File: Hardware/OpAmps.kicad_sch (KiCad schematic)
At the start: 55 parts, among them U10 TL074, U11 TL074, U12 TL074, U13 TL074, U14 TL074

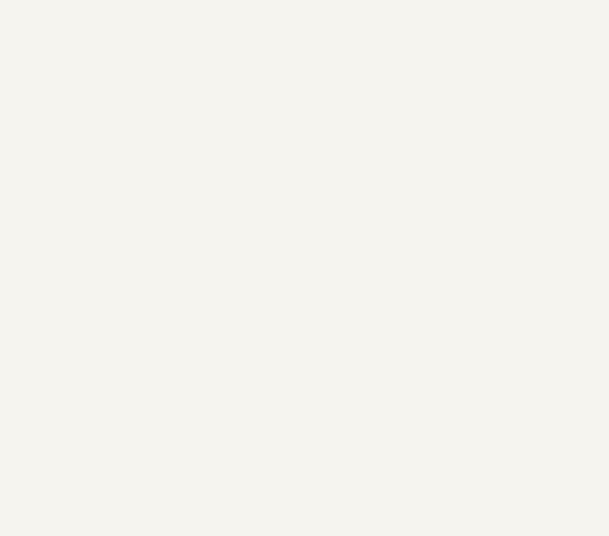
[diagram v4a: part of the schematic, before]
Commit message: Added individual audio channel breakout
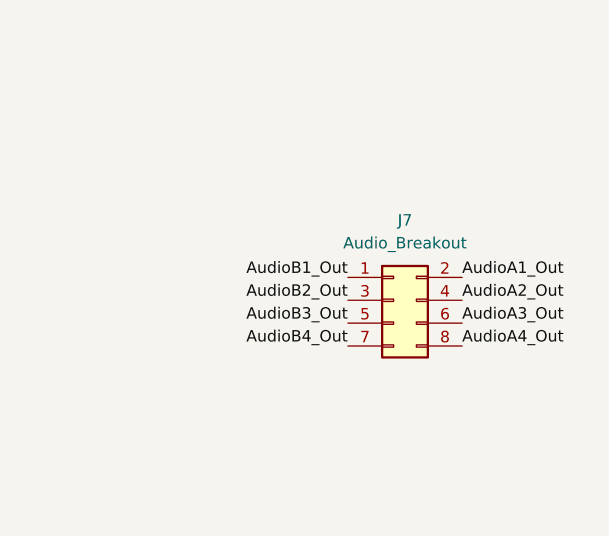
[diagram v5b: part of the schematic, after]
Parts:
- added J7: Audio_Breakout, Connector_PinHeader_2.54mm:PinHeader_2x04_P2.54mm_Vertical, symbol Connector_Generic:Conn_02x04_Odd_Even
- U14: footprint Package_SO:TSSOP-14_4.4x5mm_P0.65mm -> Package_SO:SOIC-14_3.9x8.7mm_P1.27mm
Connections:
- net AudioA1_Out: now also J7.2 (Pin_2)
- net AudioA2_Out: now also J7.4 (Pin_4)
- net AudioA3_Out: now also J7.6 (Pin_6)
- net AudioA4_Out: now also J7.8 (Pin_8)
- net AudioB1_Out: now also J7.1 (Pin_1)
- net AudioB2_Out: now also J7.3 (Pin_3)
- net AudioB3_Out: now also J7.5 (Pin_5)
- net AudioB4_Out: now also J7.7 (Pin_7)
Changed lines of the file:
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@@
     (effects (font (size 1.27 1.27)) (justify left bottom))
+  )
+  (label "AudioB1_Out" (at 358.14 184.15 180)
+    (effects (font (size 1.27 1.27)) (justify right bottom))
+  )
+  (label "AudioA3_Out" (at 370.84 189.23 0)
+    (effects (font (size 1.27 1.27)) (justify left bottom))
+  )
+  (label "AudioB3_Out" (at 358.14 189.23 180)
+    (effects (font (size 1.27 1.27)) (justify right bottom))
   )
   (label "AudioB1_Out" (at 240.03 35.56 0)
     (effects (font (size 1.27 1.27)) (justify left bottom))
   )
+  (label "AudioA2_Out" (at 370.84 186.69 0)
+    (effects (font (size 1.27 1.27)) (justify left bottom))
+  )
   (label "AudioA2_Out" (at 284.48 58.42 180)
     (effects (font (size 1.27 1.27)) (justify right bottom))
@@
     (effects (font (size 1.27 1.27)) (justify right bottom))
   )
+  (label "AudioB2_Out" (at 358.14 186.69 180)
+    (effects (font (size 1.27 1.27)) (justify right bottom))
+  )
+  (label "AudioA4_Out" (at 370.84 191.77 0)
+    (effects (font (size 1.27 1.27)) (justify left bottom))
+  )
   (label "AudioB2_Out" (at 241.3 67.31 0)
     (effects (font (size 1.27 1.27)) (justify left bottom))
@@
     (effects (font (size 1.27 1.27)) (justify left bottom))
   )
+  (label "AudioA1_Out" (at 370.84 184.15 0)
+    (effects (font (size 1.27 1.27)) (justify left bottom))
+  )
   (label "AudioA4_Out" (at 284.48 123.19 180)
     (effects (font (size 1.27 1.27)) (justify right bottom))
@@
   (label "AudioA2_Out" (at 182.88 67.31 0)
     (effects (font (size 1.27 1.27)) (justify left bottom))
+  )
+  (label "AudioB4_Out" (at 358.14 191.77 180)
+    (effects (font (size 1.27 1.27)) (justify right bottom))
   )
   (label "AudioB3_Out" (at 284.48 97.79 180)
@@
     (property "Reference" "U14" (id 0) (at 311.15 63.5 0))
     (property "Value" "TL074" (id 1) (at 311.15 71.12 0))
-    (property "Footprint" "Package_SO:TSSOP-14_4.4x5mm_P0.65mm" (id 2) (at 307.34 69.85 0)
+    (property "Footprint" "Package_SO:SOIC-14_3.9x8.7mm_P1.27mm" (id 2) (at 307.34 69.85 0)
       (effects (font (size 1.27 1.27)) hide)
     )
@@
     (pin "1")
   )
+  (symbol (lib_id "Connector_Generic:Conn_02x04_Odd_Even") (at 363.22 186.69 0) (unit 1)
+    (in_bom yes) (on_board yes) (fields_autoplaced)
+    (property "Reference" "J7" (id 0) (at 364.49 177.8 0))
+    (property "Value" "Audio_Breakout" (id 1) (at 364.49 180.34 0))
+    (property "Footprint" "Connector_PinHeader_2.54mm:PinHeader_2x04_P2.54mm_Vertical" (id 2) (at 363.22 186.69 0)
+      (effects (font (size 1.27 1.27)) hide)
+    )
+    (property "Datasheet" "~" (id 3) (at 363.22 186.69 0)
+      (effects (font (size 1.27 1.27)) hide)
+    )
+    (pin "1")
+    (pin "2")
+    (pin "3")
+    (pin "4")
+    (pin "5")
+    (pin "6")
+    (pin "7")
+    (pin "8")
+  )
   (symbol (lib_id "power:GND") (at 222.25 189.23 0) (unit 1)
     (in_bom yes) (on_board yes)
@@
     (property "Reference" "U14" (id 0) (at 306.07 185.42 0))
     (property "Value" "TL074" (id 1) (at 306.07 193.04 0))
-    (property "Footprint" "Package_SO:TSSOP-14_4.4x5mm_P0.65mm" (id 2) (at 302.26 191.77 0)
+    (property "Footprint" "Package_SO:SOIC-14_3.9x8.7mm_P1.27mm" (id 2) (at 302.26 191.77 0)
       (effects (font (size 1.27 1.27)) hide)
     )
@@
     (property "Reference" "U14" (id 0) (at 311.15 128.27 0))
     (property "Value" "TL074" (id 1) (at 311.15 135.89 0))
-    (property "Footprint" "Package_SO:TSSOP-14_4.4x5mm_P0.65mm" (id 2) (at 307.34 134.62 0)
+    (property "Footprint" "Package_SO:SOIC-14_3.9x8.7mm_P1.27mm" (id 2) (at 307.34 134.62 0)
       (effects (font (size 1.27 1.27)) hide)
     )
@@
     (property "Reference" "U14" (id 0) (at 311.15 96.52 0))
     (property "Value" "TL074" (id 1) (at 311.15 104.14 0))
-    (property "Footprint" "Package_SO:TSSOP-14_4.4x5mm_P0.65mm" (id 2) (at 307.34 102.87 0)
+    (property "Footprint" "Package_SO:SOIC-14_3.9x8.7mm_P1.27mm" (id 2) (at 307.34 102.87 0)
       (effects (font (size 1.27 1.27)) hide)
     )
@@
     (property "Reference" "U14" (id 0) (at 309.88 31.75 0))
     (property "Value" "TL074" (id 1) (at 309.88 39.37 0))
-    (property "Footprint" "Package_SO:TSSOP-14_4.4x5mm_P0.65mm" (id 2) (at 306.07 38.1 0)
-      (effects (font (size 1.27 1.27)) hide)
-    )
+    (property "Footprint" "Package_SO:SOIC-14_3.9x8.7mm_P1.27mm" (id 2) (at 306.07 38.1 0)
+      (effects (font (size 1.27 1.27)) hide)
+    )

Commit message: Routing Power traces
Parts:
- U14: footprint Package_SO:SOIC-14_3.9x8.7mm_P1.27mm -> Package_SO:TSSOP-14_4.4x5mm_P0.65mm
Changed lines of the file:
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@@
     (property "Reference" "U14" (id 0) (at 311.15 63.5 0))
     (property "Value" "TL074" (id 1) (at 311.15 71.12 0))
-    (property "Footprint" "Package_SO:SOIC-14_3.9x8.7mm_P1.27mm" (id 2) (at 307.34 69.85 0)
+    (property "Footprint" "Package_SO:TSSOP-14_4.4x5mm_P0.65mm" (id 2) (at 307.34 69.85 0)
       (effects (font (size 1.27 1.27)) hide)
     )
@@
     (property "Reference" "U14" (id 0) (at 306.07 185.42 0))
     (property "Value" "TL074" (id 1) (at 306.07 193.04 0))
-    (property "Footprint" "Package_SO:SOIC-14_3.9x8.7mm_P1.27mm" (id 2) (at 302.26 191.77 0)
+    (property "Footprint" "Package_SO:TSSOP-14_4.4x5mm_P0.65mm" (id 2) (at 302.26 191.77 0)
       (effects (font (size 1.27 1.27)) hide)
     )
@@
     (property "Reference" "U14" (id 0) (at 311.15 128.27 0))
     (property "Value" "TL074" (id 1) (at 311.15 135.89 0))
-    (property "Footprint" "Package_SO:SOIC-14_3.9x8.7mm_P1.27mm" (id 2) (at 307.34 134.62 0)
+    (property "Footprint" "Package_SO:TSSOP-14_4.4x5mm_P0.65mm" (id 2) (at 307.34 134.62 0)
       (effects (font (size 1.27 1.27)) hide)
     )
@@
     (property "Reference" "U14" (id 0) (at 311.15 96.52 0))
     (property "Value" "TL074" (id 1) (at 311.15 104.14 0))
-    (property "Footprint" "Package_SO:SOIC-14_3.9x8.7mm_P1.27mm" (id 2) (at 307.34 102.87 0)
+    (property "Footprint" "Package_SO:TSSOP-14_4.4x5mm_P0.65mm" (id 2) (at 307.34 102.87 0)
       (effects (font (size 1.27 1.27)) hide)
     )
@@
     (property "Reference" "U14" (id 0) (at 309.88 31.75 0))
     (property "Value" "TL074" (id 1) (at 309.88 39.37 0))
-    (property "Footprint" "Package_SO:SOIC-14_3.9x8.7mm_P1.27mm" (id 2) (at 306.07 38.1 0)
-      (effects (font (size 1.27 1.27)) hide)
-    )
+    (property "Footprint" "Package_SO:TSSOP-14_4.4x5mm_P0.65mm" (id 2) (at 306.07 38.1 0)
+      (effects (font (size 1.27 1.27)) hide)
+    )

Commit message: Schematic Clean Up
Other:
- note added: "Individual Audio Out"
- moved on the sheet: C37, C38, C39, C40, C41, C42, C43, C44, C45, C46, J7, R36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
